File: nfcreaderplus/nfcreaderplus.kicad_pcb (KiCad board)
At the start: 2 copper layers, 66.3 x 45.7 mm, 9 parts, among them J1 Conn_01x02, K1 G5Q-1A, U1 WeMos_D1_mini, U2 NFC_Reader_V3, U3 ULN2003

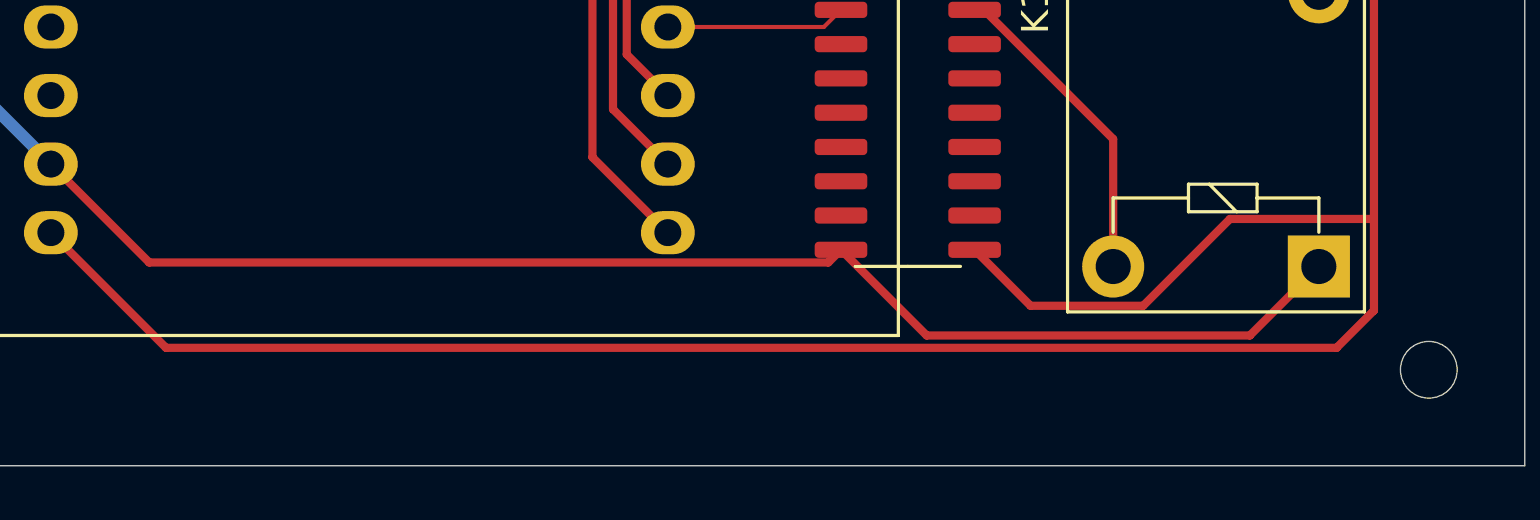
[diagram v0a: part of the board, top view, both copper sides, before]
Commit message: relay driver is grounding, pass 5V through relay then
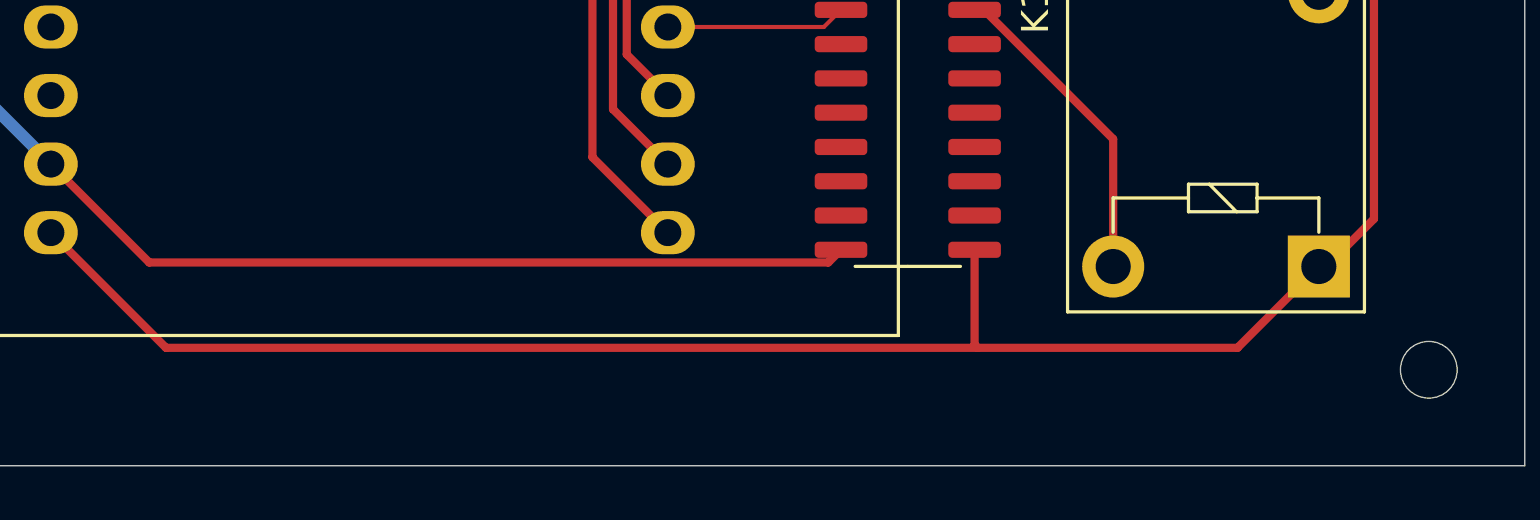
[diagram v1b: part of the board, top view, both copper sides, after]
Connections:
- K1 pad 1: GND -> 5V
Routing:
- net GND: track 130.6 -> 110.5 mm
- net 5V: track 100.9 -> 85.3 mm
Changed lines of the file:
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@@
     (descr "Through hole straight pin header, 1x02, 2.54mm pitch, single row")
     (tags "Through hole pin header THT 1x02 2.54mm single row")
-    (property "Sheetfile" "nfcreader.kicad_sch")
+    (property "Sheetfile" "nfcreaderplus.kicad_sch")
     (property "Sheetname" "")
     (attr through_hole)
@@
   (footprint "parts:NFC_Reader_V3" (layer "F.Cu")
     (at 120.301 95.25 180)
-    (property "Sheetfile" "nfcreader.kicad_sch")
+    (property "Sheetfile" "nfcreaderplus.kicad_sch")
     (property "Sheetname" "")
     (attr through_hole)
@@
   (footprint "parts:CUI_CPT-9019S-SMT" (layer "F.Cu")
     (at 121.92 66.04 180)
-    (property "Sheetfile" "nfcreader.kicad_sch")
+    (property "Sheetfile" "nfcreaderplus.kicad_sch")
     (property "Sheetname" "")
     (attr through_hole)
@@
     (descr "https://cdn-shop.adafruit.com/datasheets/WS2812B.pdf")
     (tags "LED RGB NeoPixel")
-    (property "Sheetfile" "nfcreader.kicad_sch")
+    (property "Sheetfile" "nfcreaderplus.kicad_sch")
     (property "Sheetname" "")
     (attr smd)
@@
     (descr "Relay SPST-NO Omron Serie G5Q, http://omronfs.omron.com/en_US/ecb/products/pdf/en-g5q.pdf")
     (tags "Relay SPST-NO Omron Serie G5Q")
-    (property "Sheetfile" "nfcreader.kicad_sch")
+    (property "Sheetfile" "nfcreaderplus.kicad_sch")
     (property "Sheetname" "")
     (attr through_hole)
@@
     (fp_line (start -1.18 -8.81) (end 18.96 -8.81) (layer "F.Fab") (width 0.1))
     (pad "1" thru_hole rect (at 0 0 270) (size 2.3 2.3) (drill 1.3) (layers *.Cu *.Mask)
-      (net 6 "GND") (pintype "passive"))
+      (net 4 "5V") (pintype "passive"))
     (pad "2" thru_hole circle (at 10.16 0 270) (size 2.3 2.3) (drill 1.3) (layers *.Cu *.Mask)
       (net 39 "Net-(J1-Pad2)") (pintype "passive"))
@@
     (descr "Mounting Hole 2.1mm, no annular")
     (tags "mounting hole 2.1mm no annular")
-    (property "Sheetfile" "nfcreader.kicad_sch")
+    (property "Sheetfile" "nfcreaderplus.kicad_sch")
     (property "Sheetname" "")
     (attr exclude_from_pos_files)
@@
     (descr "SOIC, 16 Pin (JEDEC MS-012AC, https://www.analog.com/media/en/package-pcb-resources/package/pkg_pdf/soic_narrow-r/r_16.pdf), generated with kicad-footprint-generator ipc_gullwing_generator.py")
     (tags "SOIC SO")
-    (property "Sheetfile" "nfcreader.kicad_sch")
+    (property "Sheetfile" "nfcreaderplus.kicad_sch")
     (property "Sheetname" "")
     (attr smd)
@@
     (descr "Mounting Hole 2.1mm, no annular")
     (tags "mounting hole 2.1mm no annular")
-    (property "Sheetfile" "nfcreader.kicad_sch")
+    (property "Sheetfile" "nfcreaderplus.kicad_sch")
     (property "Sheetname" "")
     (attr exclude_from_pos_files)
@@
     (descr "16-pin module, column spacing 22.86 mm (900 mils), https://wiki.wemos.cc/products:d1:d1_mini, https://c1.staticflickr.com/1/734/31400410271_f278b087db_z.jpg")
     (tags "ESP8266 WiFi microcontroller")
-    (property "Sheetfile" "nfcreader.kicad_sch")
+    (property "Sheetfile" "nfcreaderplus.kicad_sch")
     (property "Sheetname" "")
     (attr through_hole)
@@
   )
   (gr_rect (start 77.216 54.356) (end 143.51 100.076) (layer "Edge.Cuts") (width 0.05) (fill none))
-  (segment (start 132.588 90.932) (end 129.3702 94.1498) (width 0.3048) (layer "F.Cu") (net 4))
+  (segment (start 123.125 92.075) (end 123.125 95.591398) (width 0.3048) (layer "F.Cu") (net 4))
   (segment (start 137.922 62.012) (end 138.086 61.848) (width 0.3048) (layer "F.Cu") (net 4))
-  (segment (start 129.3702 94.1498) (end 125.1998 94.1498) (width 0.3048) (layer "F.Cu") (net 4))
-  (segment (start 93.167199 95.707199) (end 136.540401 95.707199) (width 0.3048) (layer "F.Cu") (net 4))
-  (segment (start 136.540401 95.707199) (end 137.922 94.3256) (width 0.3048) (layer "F.Cu") (net 4))
-  (segment (start 125.1998 94.1498) (end 123.125 92.075) (width 0.3048) (layer "F.Cu") (net 4))
+  (segment (start 123.125 95.591398) (end 123.240801 95.707199) (width 0.3048) (layer "F.Cu") (net 4))
+  (segment (start 137.922 90.932) (end 136.159 92.695) (width 0.3048) (layer "F.Cu") (net 4))
   (segment (start 137.922 90.932) (end 137.922 62.012) (width 0.3048) (layer "F.Cu") (net 4))
+  (segment (start 132.867801 95.707199) (end 123.240801 95.707199) (width 0.3048) (layer "F.Cu") (net 4))
+  (segment (start 123.240801 95.707199) (end 93.167199 95.707199) (width 0.3048) (layer "F.Cu") (net 4))
+  (segment (start 135.88 92.695) (end 132.867801 95.707199) (width 0.3048) (layer "F.Cu") (net 4))
   (segment (start 88.9 91.44) (end 93.167199 95.707199) (width 0.3048) (layer "F.Cu") (net 4))
-  (segment (start 137.922 94.3256) (end 137.922 90.932) (width 0.3048) (layer "F.Cu") (net 4))
-  (segment (start 137.922 90.932) (end 132.588 90.932) (width 0.3048) (layer "F.Cu") (net 4))
   (segment (start 121.92 62.04) (end 129.694 62.04) (width 0.3048) (layer "F.Cu") (net 6))
-  (segment (start 121.35 95.25) (end 133.325 95.25) (width 0.3048) (layer "F.Cu") (net 6))
   (segment (start 129.694 62.04) (end 133.186 58.548) (width 0.3048) (layer "F.Cu") (net 6))
-  (segment (start 118.175 92.075) (end 121.35 95.25) (width 0.3048) (layer "F.Cu") (net 6))
   (segment (start 118.175 92.075) (end 117.7052 92.5448) (width 0.3048) (layer "F.Cu") (net 6))
-  (segment (start 133.325 95.25) (end 135.88 92.695) (width 0.3048) (layer "F.Cu") (net 6))
   (segment (start 106.839 62.738) (end 121.222 62.738) (width 0.3048) (layer "F.Cu") (net 6))
   (segment (start 121.222 62.738) (end 121.92 62.04) (width 0.3048) (layer "F.Cu") (net 6))
